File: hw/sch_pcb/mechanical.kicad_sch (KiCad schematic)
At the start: 9 parts

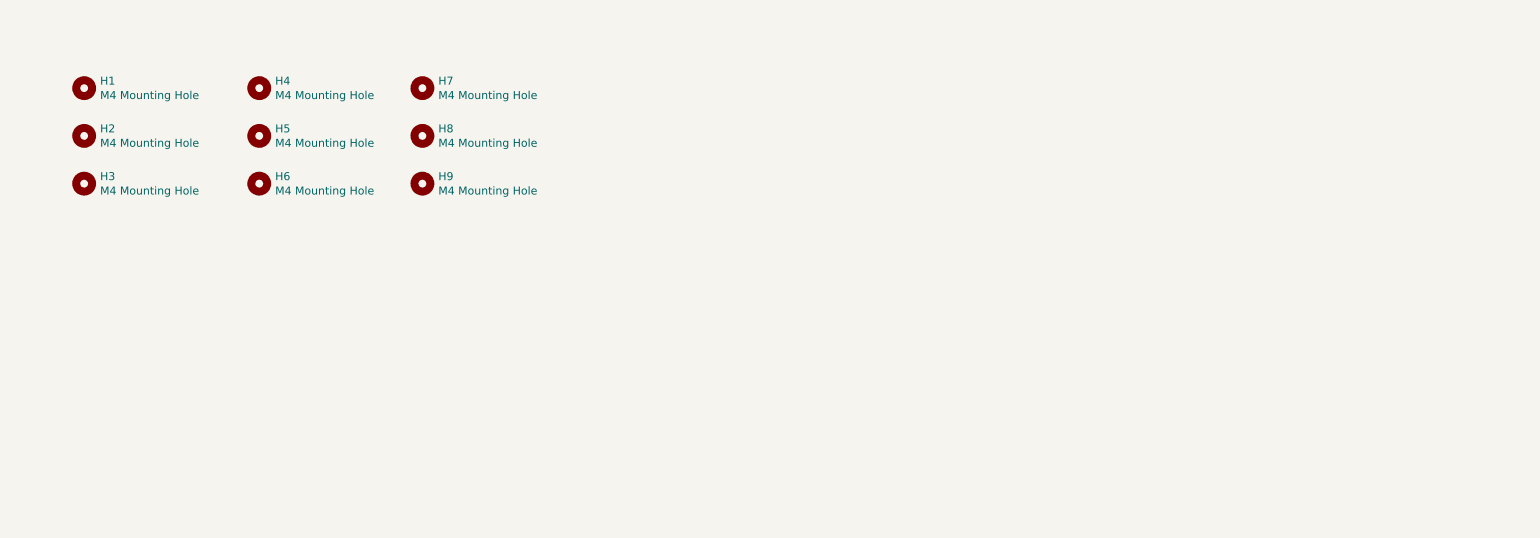
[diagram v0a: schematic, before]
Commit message: Add print plate arangement screws.
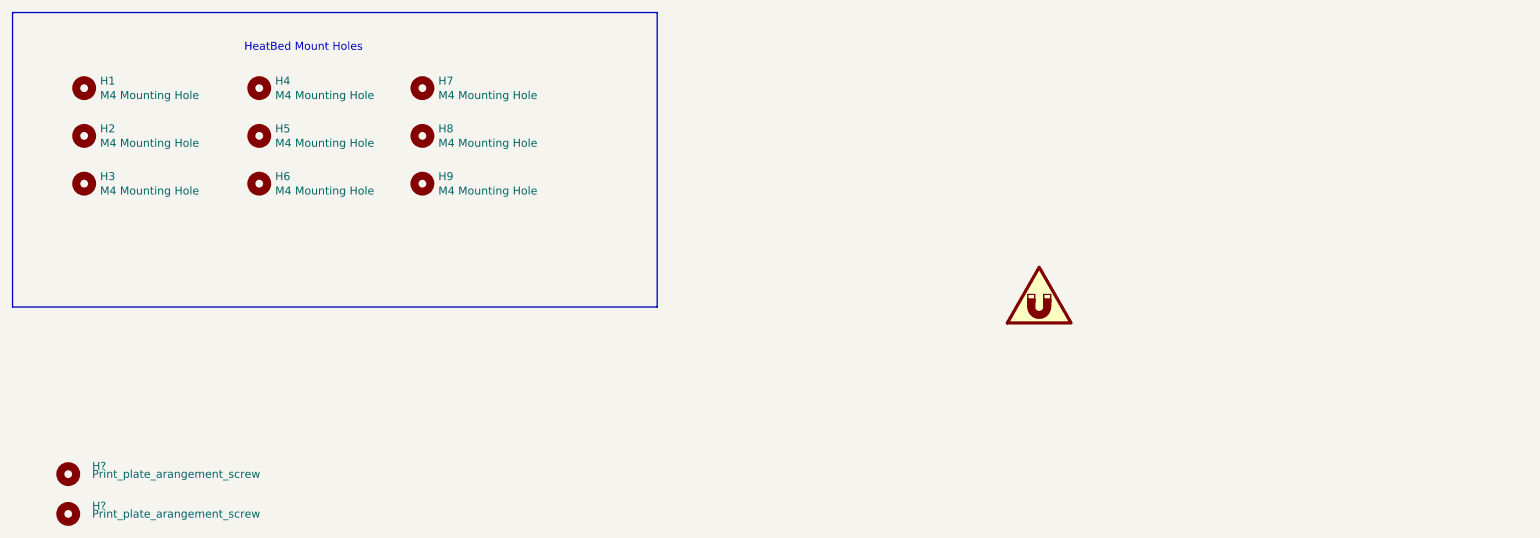
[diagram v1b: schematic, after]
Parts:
- added H? (x2): Print_plate_arangement_screw, MountingHole:MountingHole_3.2mm_M3_ISO14580, symbol Mechanical:MountingHole
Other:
- note added: "HeatBed Mount Holes"
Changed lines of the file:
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@@
   (page 2 2)
   (paper "A4")
+  (polyline (pts (xy 26.67 20.32) (xy 26.67 67.31))
+    (stroke (width 0) (type solid) (color 0 0 0 0))
+  )
+  (polyline (pts (xy 26.67 20.32) (xy 129.54 20.32))
+    (stroke (width 0) (type solid) (color 0 0 0 0))
+  )
+  (polyline (pts (xy 129.54 20.32) (xy 129.54 67.31))
+    (stroke (width 0) (type solid) (color 0 0 0 0))
+  )
+  (polyline (pts (xy 129.54 67.31) (xy 26.67 67.31))
+    (stroke (width 0) (type solid) (color 0 0 0 0))
+  )
+  (text "HeatBed Mount Holes" (at 82.55 26.67 180)
+    (effects (font (size 1.27 1.27)) (justify right bottom))
+  )
+  (symbol (lib_id "Mechanical:MountingHole") (at 35.56 93.98 0) (unit 1)
+    (in_bom yes) (on_board yes)
+    (property "Reference" "H?" (id 0) (at 39.37 92.71 0)
+      (effects (font (size 1.27 1.27)) (justify left))
+    )
+    (property "Value" "Print_plate_arangement_screw" (id 1) (at 39.37 93.98 0)
+      (effects (font (size 1.27 1.27)) (justify left))
+    )
+    (property "Footprint" "MountingHole:MountingHole_3.2mm_M3_ISO14580" (id 2) (at 35.56 93.98 0)
+      (effects (font (size 1.27 1.27)) hide)
+    )
+    (property "Datasheet" "~" (id 3) (at 35.56 93.98 0)
+      (effects (font (size 1.27 1.27)) hide)
+    )
+  )
+  (symbol (lib_id "Mechanical:MountingHole") (at 35.56 100.33 0) (unit 1)
+    (in_bom yes) (on_board yes)
+    (property "Reference" "H?" (id 0) (at 39.37 99.06 0)
+      (effects (font (size 1.27 1.27)) (justify left))
+    )
+    (property "Value" "Print_plate_arangement_screw" (id 1) (at 39.37 100.33 0)
+      (effects (font (size 1.27 1.27)) (justify left))
+    )
+    (property "Footprint" "MountingHole:MountingHole_3.2mm_M3_ISO14580" (id 2) (at 35.56 100.33 0)
+      (effects (font (size 1.27 1.27)) hide)
+    )
+    (property "Datasheet" "~" (id 3) (at 35.56 100.33 0)
+      (effects (font (size 1.27 1.27)) hide)
+    )
+  )
   (symbol (lib_id "Mechanical:MountingHole") (at 38.1 32.385 0) (unit 1)
     (in_bom yes) (on_board yes)
@@
       (effects (font (size 1.27 1.27)) hide)
     )
+  )
+  (symbol (lib_id "Graphic:SYM_Magnet_Large") (at 190.5 64.77 0) (unit 1)
+    (in_bom yes) (on_board yes)
+    (property "Reference" "#SYM?" (id 0) (at 190.5 59.69 0)
+      (effects (font (size 1.27 1.27)) hide)
+    )
+    (property "Value" "SYM_Magnet_Large" (id 1) (at 190.5 71.12 0)
+      (effects (font (size 1.27 1.27)) hide)
+    )
+    (property "Footprint" "" (id 2) (at 190.5 69.85 0)
+      (effects (font (size 1.27 1.27)) hide)
+    )
+    (property "Datasheet" "~" (id 3) (at 191.262 69.85 0)
+      (effects (font (size 1.27 1.27)) hide)
+    )

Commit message: Magnets handled as PCB components.
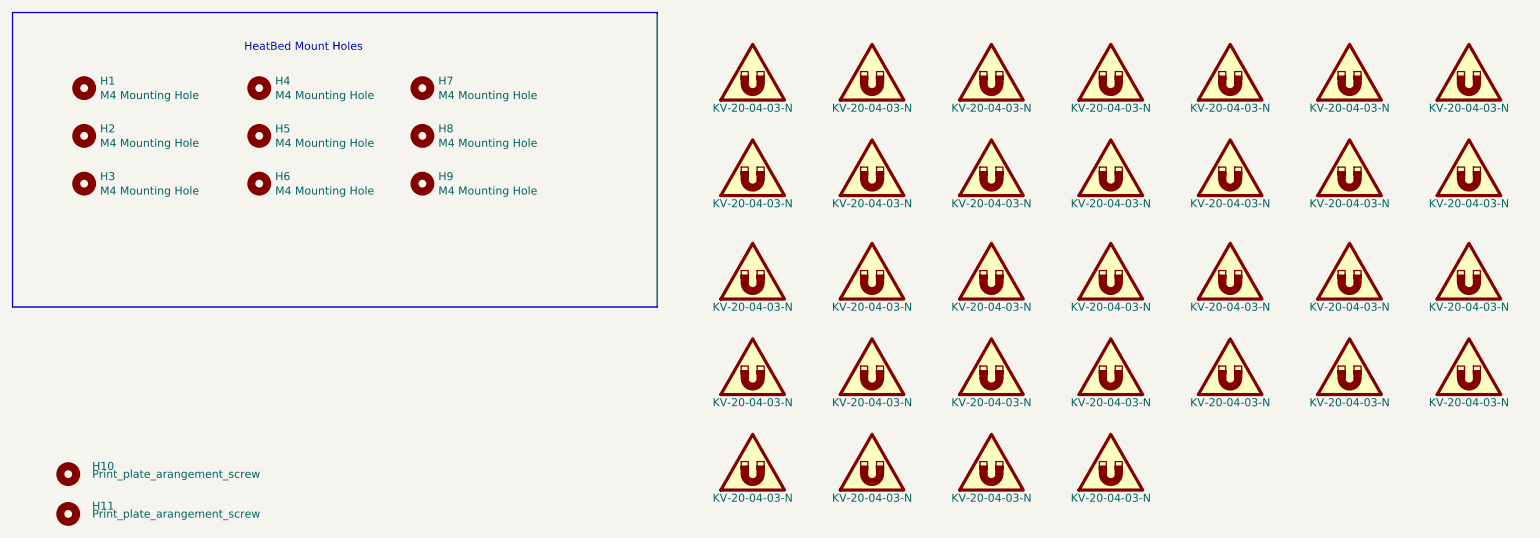
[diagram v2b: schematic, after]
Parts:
- added M1, M10, M11, M12, M13, M14, M15, M16, M17, M18, M19, M2, M20, M21, M22, M23, M24, M26, M27, M28, M29, M3, M31, M32, M33, M34, M4, M5, M6, M7, M8, M9: KV-20-04-03-N, local_lib:KV-20-04-03-N, symbol Graphic:SYM_Magnet_Large
- H1, H2, H3, H4, H5, H6, H7, H8, H9: footprint MountingHole:MountingHole_4.3mm_M4_DIN965 -> MountingHole:MountingHole_4.3mm_M4
- gave numbers to parts that had none: 2

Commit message: Zones edits and routing.
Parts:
- H1, H2, H3, H4, H5, H6, H7, H8, H9: footprint MountingHole:MountingHole_4.3mm_M4 -> local_lib:MountingHole_4.3mm_M4
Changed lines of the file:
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@@
       (effects (font (size 1.27 1.27)) (justify left))
     )
-    (property "Footprint" "MountingHole:MountingHole_4.3mm_M4" (id 2) (at 38.1 32.385 0)
+    (property "Footprint" "local_lib:MountingHole_4.3mm_M4" (id 2) (at 38.1 32.385 0)
       (effects (font (size 1.27 1.27)) hide)
     )
@@
       (effects (font (size 1.27 1.27)) (justify left))
     )
-    (property "Footprint" "MountingHole:MountingHole_4.3mm_M4" (id 2) (at 38.1 40.005 0)
+    (property "Footprint" "local_lib:MountingHole_4.3mm_M4" (id 2) (at 38.1 40.005 0)
       (effects (font (size 1.27 1.27)) hide)
     )
@@
       (effects (font (size 1.27 1.27)) (justify left))
     )
-    (property "Footprint" "MountingHole:MountingHole_4.3mm_M4" (id 2) (at 38.1 47.625 0)
+    (property "Footprint" "local_lib:MountingHole_4.3mm_M4" (id 2) (at 38.1 47.625 0)
       (effects (font (size 1.27 1.27)) hide)
     )
@@
       (effects (font (size 1.27 1.27)) (justify left))
     )
-    (property "Footprint" "MountingHole:MountingHole_4.3mm_M4" (id 2) (at 66.04 32.385 0)
+    (property "Footprint" "local_lib:MountingHole_4.3mm_M4" (id 2) (at 66.04 32.385 0)
       (effects (font (size 1.27 1.27)) hide)
     )
@@
       (effects (font (size 1.27 1.27)) (justify left))
     )
-    (property "Footprint" "MountingHole:MountingHole_4.3mm_M4" (id 2) (at 66.04 40.005 0)
+    (property "Footprint" "local_lib:MountingHole_4.3mm_M4" (id 2) (at 66.04 40.005 0)
       (effects (font (size 1.27 1.27)) hide)
     )
@@
       (effects (font (size 1.27 1.27)) (justify left))
     )
-    (property "Footprint" "MountingHole:MountingHole_4.3mm_M4" (id 2) (at 66.04 47.625 0)
+    (property "Footprint" "local_lib:MountingHole_4.3mm_M4" (id 2) (at 66.04 47.625 0)
       (effects (font (size 1.27 1.27)) hide)
     )
@@
       (effects (font (size 1.27 1.27)) (justify left))
     )
-    (property "Footprint" "MountingHole:MountingHole_4.3mm_M4" (id 2) (at 92.075 32.385 0)
+    (property "Footprint" "local_lib:MountingHole_4.3mm_M4" (id 2) (at 92.075 32.385 0)
       (effects (font (size 1.27 1.27)) hide)
     )
@@
       (effects (font (size 1.27 1.27)) (justify left))
     )
-    (property "Footprint" "MountingHole:MountingHole_4.3mm_M4" (id 2) (at 92.075 40.005 0)
+    (property "Footprint" "local_lib:MountingHole_4.3mm_M4" (id 2) (at 92.075 40.005 0)
       (effects (font (size 1.27 1.27)) hide)
     )
@@
       (effects (font (size 1.27 1.27)) (justify left))
     )
-    (property "Footprint" "MountingHole:MountingHole_4.3mm_M4" (id 2) (at 92.075 47.625 0)
+    (property "Footprint" "local_lib:MountingHole_4.3mm_M4" (id 2) (at 92.075 47.625 0)
       (effects (font (size 1.27 1.27)) hide)
     )

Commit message: Zone infill improvement.
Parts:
- H10, H11: footprint MountingHole:MountingHole_3.2mm_M3_ISO14580 -> local_lib:MountingHole_3.2mm_M3_ISO14580
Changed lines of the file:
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@@
       (effects (font (size 1.27 1.27)) (justify left))
     )
-    (property "Footprint" "MountingHole:MountingHole_3.2mm_M3_ISO14580" (id 2) (at 35.56 93.98 0)
+    (property "Footprint" "local_lib:MountingHole_3.2mm_M3_ISO14580" (id 2) (at 35.56 93.98 0)
       (effects (font (size 1.27 1.27)) hide)
     )
@@
       (effects (font (size 1.27 1.27)) (justify left))
     )
-    (property "Footprint" "MountingHole:MountingHole_3.2mm_M3_ISO14580" (id 2) (at 35.56 100.33 0)
+    (property "Footprint" "local_lib:MountingHole_3.2mm_M3_ISO14580" (id 2) (at 35.56 100.33 0)
       (effects (font (size 1.27 1.27)) hide)
     )
